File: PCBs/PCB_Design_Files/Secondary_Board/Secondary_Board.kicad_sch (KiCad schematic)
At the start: 0 parts

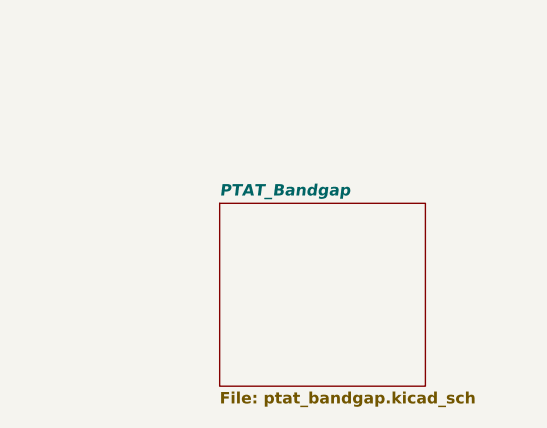
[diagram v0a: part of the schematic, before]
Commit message: ptat_bandgap schematic on secondary board
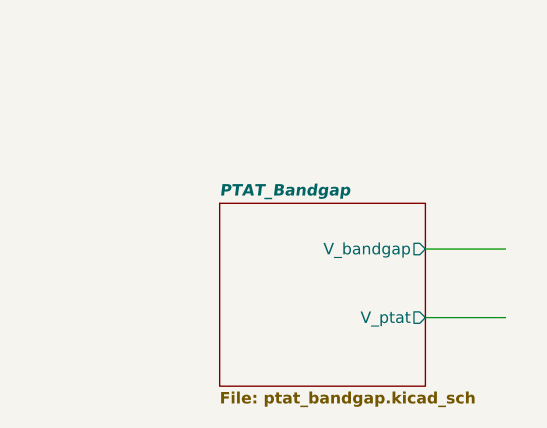
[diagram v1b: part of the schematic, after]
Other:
- sheet PTAT_Bandgap ports: added V_bandgap, V_ptat; removed none
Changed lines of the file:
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@@
+		)
+	)
+	(wire
+		(pts
+			(xy 228.6 85.09) (xy 237.49 85.09)
+		)
+		(stroke
+			(width 0)
+			(type default)
+		)
+	)
+	(wire
+		(pts
+			(xy 228.6 92.71) (xy 237.49 92.71)
+		)
+		(stroke
+			(width 0)
+			(type default)
 		)
 	)
@@
 			)
 		)
+		(pin "V_bandgap" output
+			(at 228.6 85.09 0)
+			(effects
+				(font
+					(size 1.27 1.27)
+				)
+				(justify right)
+			)
+		)
+		(pin "V_ptat" output
+			(at 228.6 92.71 0)
+			(effects
+				(font
+					(size 1.27 1.27)
+				)
+				(justify right)
+			)
+		)

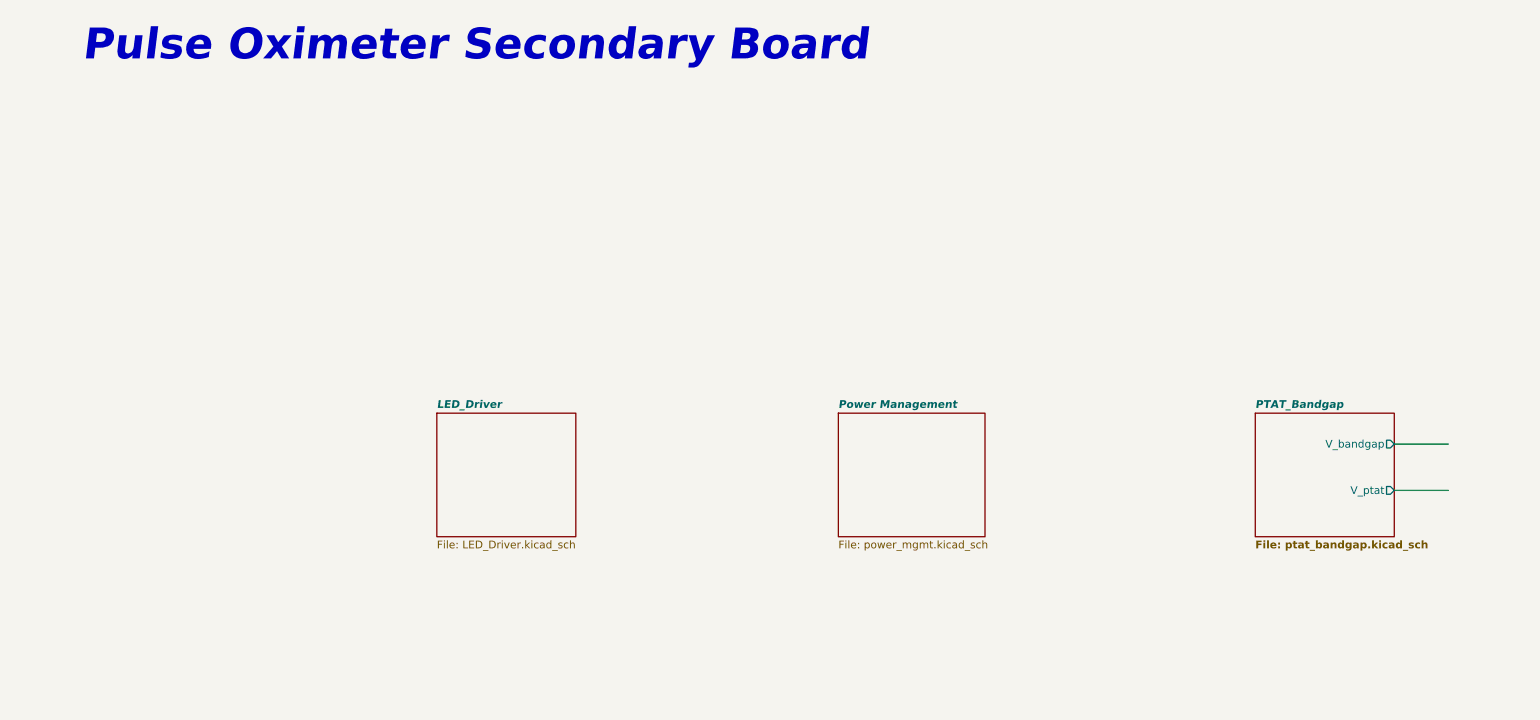
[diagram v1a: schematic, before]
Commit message: Bandgap/Ptat layout on secondary board. Updated grounded mounting holes on schematic, fix all DRC warnings
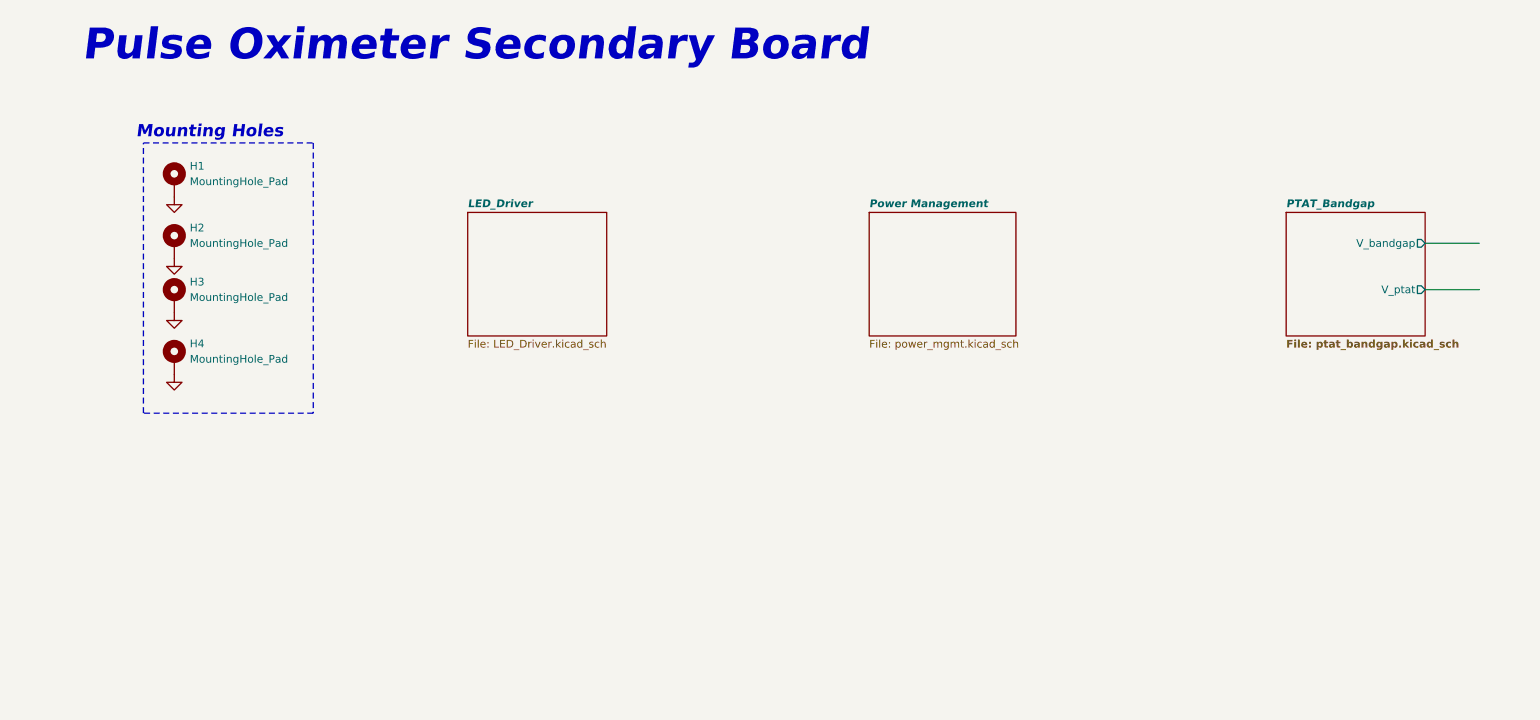
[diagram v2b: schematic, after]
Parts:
- added H1, H2, H3, H4: MountingHole_Pad, MountingHole:MountingHole_2.2mm_M2_DIN965_Pad, symbol Mechanical:MountingHole_Pad
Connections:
- new net GND: H1.1, H2.1, H3.1, H4.1
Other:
- note added: "Mounting Holes"

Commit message: Added header and ffc connector to both boards + update libraries. Updated BOM
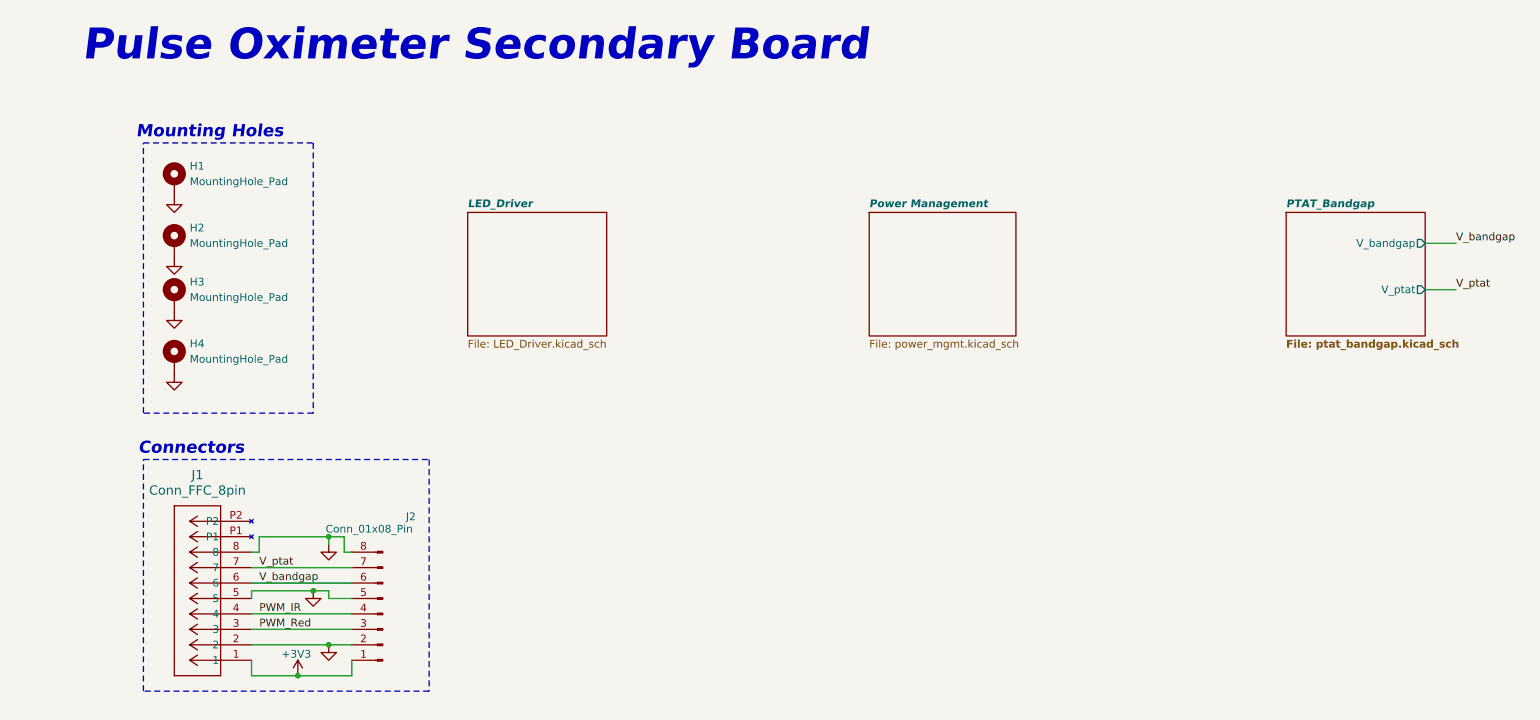
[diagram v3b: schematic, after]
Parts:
- added J1: Conn_FFC_8pin, Project Footprints:Conn_FFC_8pin, symbol Project_Symbols:Conn_FFC_8pin
- added J2: Conn_01x08_Pin, Connector_PinHeader_2.54mm:PinHeader_1x08_P2.54mm_Vertical, symbol Connector:Conn_01x08_Pin
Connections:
- net GND: now also J1.2, J1.5, J1.8, J2.2 (Pin_2), J2.5 (Pin_5), J2.8 (Pin_8)
- new net +3V3: J1.1, J2.1 (Pin_1)
- new net PWM_IR: J1.4, J2.4 (Pin_4)
- new net PWM_Red: J1.3, J2.3 (Pin_3)
- new net V_bandgap: J1.6, J2.6 (Pin_6)
- new net V_ptat: J1.7, J2.7 (Pin_7)
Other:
- note added: "Connectors"

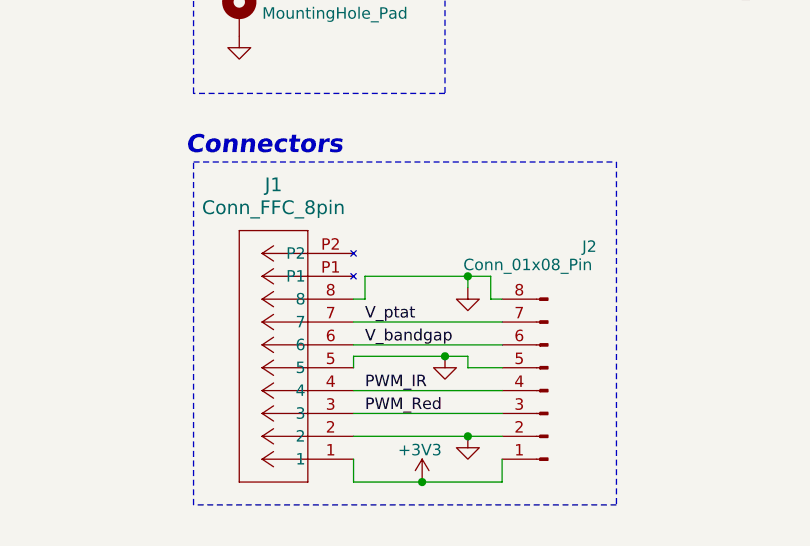
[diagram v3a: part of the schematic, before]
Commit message: pin 2 5V
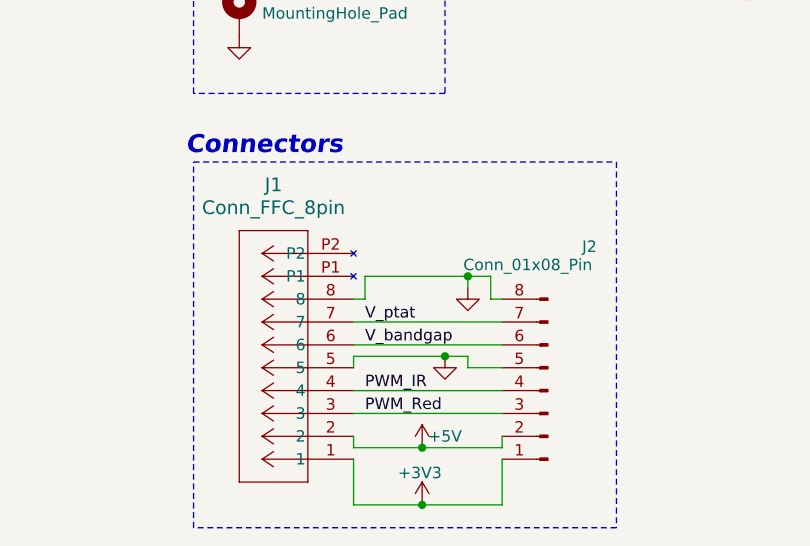
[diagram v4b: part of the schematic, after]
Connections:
- net GND: no longer J1.2, J2.2 (Pin_2)
- new net +5V: J1.2, J2.2 (Pin_2)
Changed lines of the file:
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@@
 	(rectangle
 		(start 22.86 87.63)
-		(end 69.85 125.73)
+		(end 69.85 128.27)
 		(stroke
 			(width 0)
@@
 	)
 	(junction
-		(at 48.26 123.19)
+		(at 50.8 109.22)
 		(diameter 0)
 		(color 0 0 0 0)
 	)
 	(junction
-		(at 50.8 109.22)
+		(at 48.26 119.38)
 		(diameter 0)
 		(color 0 0 0 0)
@@
 	)
 	(junction
-		(at 53.34 118.11)
+		(at 48.26 125.73)
 		(diameter 0)
 		(color 0 0 0 0)
@@
 	(wire
 		(pts
+			(xy 48.26 119.38) (xy 57.15 119.38)
+		)
+		(stroke
+			(width 0)
+			(type default)
+		)
+	)
+	(wire
+		(pts
 			(xy 50.8 109.22) (xy 53.34 109.22)
 		)
@@
 	(wire
 		(pts
-			(xy 40.64 120.65) (xy 40.64 123.19)
+			(xy 40.64 120.65) (xy 40.64 125.73)
 		)
 		(stroke
@@
 	(wire
 		(pts
-			(xy 40.64 123.19) (xy 48.26 123.19)
+			(xy 40.64 125.73) (xy 48.26 125.73)
 		)
 		(stroke
@@
 	(wire
 		(pts
-			(xy 57.15 123.19) (xy 48.26 123.19)
-		)
-		(stroke
-			(width 0)
-			(type default)
-		)
-	)
-	(wire
-		(pts
-			(xy 57.15 120.65) (xy 57.15 123.19)
+			(xy 57.15 125.73) (xy 48.26 125.73)
+		)
+		(stroke
+			(width 0)
+			(type default)
+		)
+	)
+	(wire
+		(pts
+			(xy 57.15 120.65) (xy 57.15 125.73)
 		)
 		(stroke
@@
 	(wire
 		(pts
-			(xy 53.34 118.11) (xy 57.15 118.11)
+			(xy 40.64 119.38) (xy 40.64 118.11)
 		)
 		(stroke
@@
 	(wire
 		(pts
-			(xy 40.64 118.11) (xy 53.34 118.11)
+			(xy 40.64 119.38) (xy 48.26 119.38)
+		)
+		(stroke
+			(width 0)
+			(type default)
+		)
+	)
+	(wire
+		(pts
+			(xy 57.15 119.38) (xy 57.15 118.11)
 		)
 		(stroke
@@
 	(symbol
 		(lib_id "power:+3V3")
-		(at 48.26 123.19 0)
+		(at 48.26 125.73 0)
 		(unit 1)
 		(exclude_from_sim no)
@@
 		(dnp no)
 		(property "Reference" "#PWR014"
-			(at 48.26 127 0)
+			(at 48.26 129.54 0)
 			(effects
 				(font
@@
 		)
 		(property "Value" "+3V3"
-			(at 48.006 119.634 0)
+			(at 48.006 122.174 0)
 			(effects
 				(font
@@
 		)
 		(property "Footprint" ""
-			(at 48.26 123.19 0)
+			(at 48.26 125.73 0)
 			(effects
 				(font
@@
 		)
 		(property "Datasheet" ""
-			(at 48.26 123.19 0)
+			(at 48.26 125.73 0)
 			(effects
 				(font
@@
 		)
 		(property "Description" "Power symbol creates a global label with name \"+3V3\""
-			(at 48.26 123.19 0)
+			(at 48.26 125.73 0)
 			(effects
 				(font
@@
 				(path "/2f5986e4-77b2-4f5d-ab91-80ba6228eb8b"
 					(reference "#PWR014")
-					(unit 1)
-				)
-			)
-		)
-	)
-	(symbol
-		(lib_id "power:GND")
-		(at 53.34 118.11 0)
-		(unit 1)
-		(exclude_from_sim no)
-		(in_bom yes)
-		(on_board yes)
-		(dnp no)
-		(fields_autoplaced yes)
-		(property "Reference" "#PWR017"
-			(at 53.34 124.46 0)
-			(effects
-				(font
-					(size 1.27 1.27)
-				)
-				(hide yes)
-			)
-		)
-		(property "Value" "GND"
-			(at 53.3401 121.92 90)
-			(effects
-				(font
-					(size 1.27 1.27)
-				)
-				(justify right)
-				(hide yes)
-			)
-		)
-		(property "Footprint" ""
-			(at 53.34 118.11 0)
-			(effects
-				(font
-					(size 1.27 1.27)
-				)
-				(hide yes)
-			)
-		)
-		(property "Datasheet" ""
-			(at 53.34 118.11 0)
-			(effects
-				(font
-					(size 1.27 1.27)
-				)
-				(hide yes)
-			)
-		)
-		(property "Description" "Power symbol creates a global label with name \"GND\" , ground"
-			(at 53.34 118.11 0)
-			(effects
-				(font
-					(size 1.27 1.27)
-				)
-				(hide yes)
-			)
-		)
-		(pin "1"
-		)
-		(instances
-			(project "Secondary_Board"
-				(path "/2f5986e4-77b2-4f5d-ab91-80ba6228eb8b"
-					(reference "#PWR017")
 					(unit 1)
 				)
@@
 					(unit 1)
 				)
+			)
+		)
+	)
+	(symbol
+		(lib_id "power:VCC")
+		(at 48.26 119.38 0)
+		(unit 1)
+		(exclude_from_sim no)
+		(in_bom yes)
+		(on_board yes)
+		(dnp no)
+		(property "Reference" "#PWR017"
+			(at 48.26 123.19 0)
+			(effects
+				(font
+					(size 1.27 1.27)
+				)
+				(hide yes)
+			)
+		)
+		(property "Value" "+5V"
+			(at 50.8 118.11 0)
+			(effects
+				(font
+					(size 1.27 1.27)
+				)
+			)
+		)
+		(property "Footprint" ""
+			(at 48.26 119.38 0)
+			(effects
+				(font
+					(size 1.27 1.27)
+				)
+				(hide yes)
+			)
+		)
+		(property "Datasheet" ""
+			(at 48.26 119.38 0)
+			(effects
+				(font
+					(size 1.27 1.27)
+				)
+				(hide yes)
+			)
+		)
+		(property "Description" "Power symbol creates a global label with name \"VCC\""
+			(at 48.26 119.38 0)
+			(effects
+				(font
+					(size 1.27 1.27)
+				)
+				(hide yes)
+			)
+		)
+		(pin "1"
+		)
+		(instances
+			(project "Secondary_Board"
+				(path "/2f5986e4-77b2-4f5d-ab91-80ba6228eb8b"
+					(reference "#PWR017")
+					(unit 1)
+				)

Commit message: updated bg_ptat
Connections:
- net V_bandgap: now also J1.7, J2.7 (Pin_7); no longer J1.6, J2.6 (Pin_6)
- net V_ptat: now also J1.6, J2.6 (Pin_6); no longer J1.7, J2.7 (Pin_7)
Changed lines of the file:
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@@
 		)
 	)
-	(label "V_bandgap"
+	(label "V_ptat"
 		(at 41.91 107.95 0)
 		(effects
@@
 	)
 	(label "V_bandgap"
+		(at 41.91 105.41 0)
+		(effects
+			(font
+				(size 1.27 1.27)
+			)
+			(justify left bottom)
+		)
+	)
+	(label "V_bandgap"
 		(at 238.76 52.07 0)
 		(effects
@@
 		(effects
 			(font
-				(size 1.27 1.27)
-			)
-			(justify left bottom)
-		)
-	)
-	(label "V_ptat"
-		(at 41.91 105.41 0)
-		(effects
-			(font

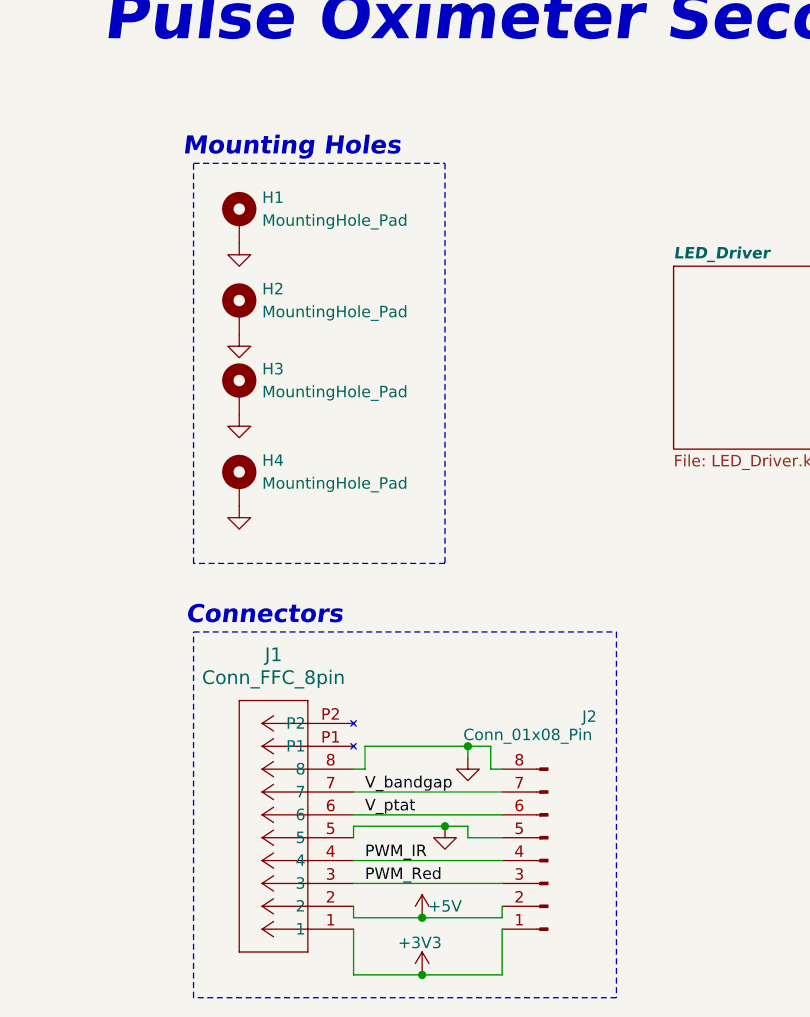
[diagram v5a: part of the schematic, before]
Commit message: connected connectors
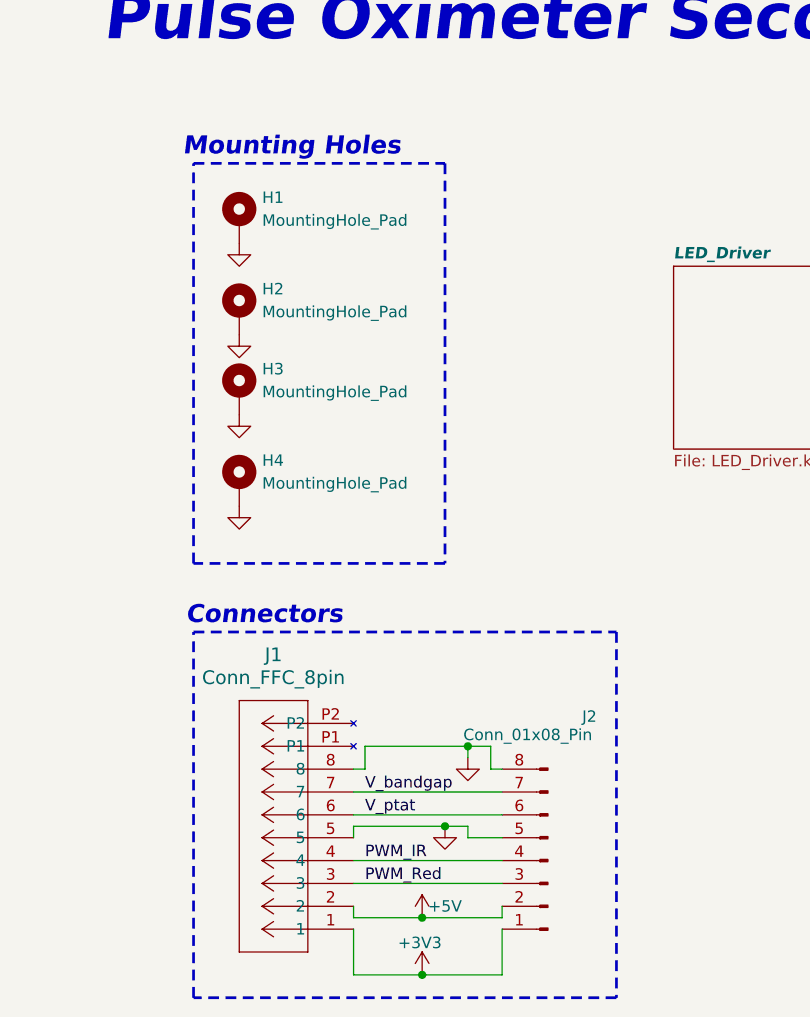
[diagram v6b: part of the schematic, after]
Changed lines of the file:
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@@
 		(end 50.8 80.01)
 		(stroke
-			(width 0)
+			(width 0.3)
 			(type dash)
+			(color 0 0 0 1)
 		)
 		(fill
@@
 		(end 69.85 128.27)
 		(stroke
-			(width 0)
+			(width 0.3)
 			(type dash)
+			(color 0 0 0 1)
 		)
 		(fill

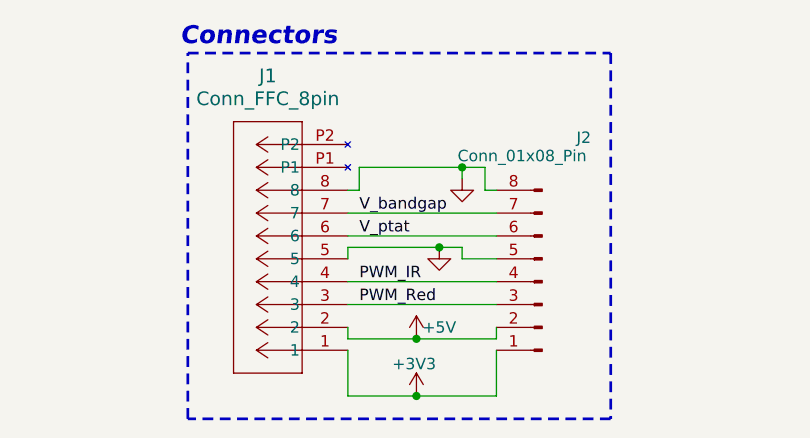
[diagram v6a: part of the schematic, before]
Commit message: LED Driver added to PCB
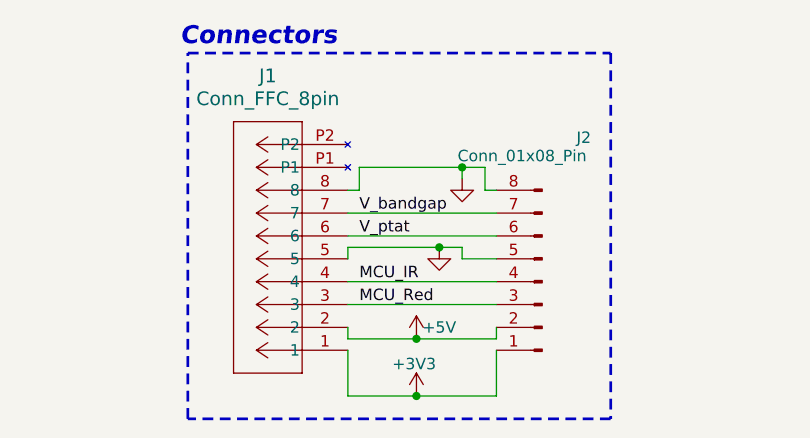
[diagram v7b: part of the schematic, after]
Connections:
- net PWM_IR renamed MCU_IR
- net PWM_Red renamed MCU_Red
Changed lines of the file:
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@@
 		)
 	)
-	(label "PWM_IR"
+	(label "MCU_IR"
 		(at 41.91 113.03 0)
 		(effects
@@
 		)
 	)
-	(label "PWM_Red"
+	(label "MCU_Red"
 		(at 41.91 115.57 0)
 		(effects

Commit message: LED Driver Updates
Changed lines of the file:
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@@
-		)
-	)
-	(label "MCU_IR"
-		(at 41.91 113.03 0)
-		(effects
-			(font
-				(size 1.27 1.27)
-			)
-			(justify left bottom)
 		)
 	)
@@
 		)
 	)
-	(label "MCU_Red"
-		(at 41.91 115.57 0)
+	(global_label "MCU_IR"
+		(shape input)
+		(at 41.91 113.03 180)
+		(fields_autoplaced yes)
 		(effects
 			(font
 				(size 1.27 1.27)
 			)
-			(justify left bottom)
+			(justify right)
+		)
+		(property "Intersheetrefs" "${INTERSHEET_REFS}"
+			(at 32.0305 113.03 0)
+			(effects
+				(font
+					(size 1.27 1.27)
+				)
+				(justify right)
+				(hide yes)
+			)
 		)
 	)
+	(global_label "MCU_Red"
+		(shape input)
+		(at 41.91 115.57 180)
+		(fields_autoplaced yes)
+		(effects
+			(font
+				(size 1.27 1.27)
+			)
+			(justify right)
+		)
+		(property "Intersheetrefs" "${INTERSHEET_REFS}"
+			(at 30.3977 115.57 0)
+			(effects
+				(font
+					(size 1.27 1.27)
+				)
+				(justify right)
+				(hide yes)
+			)
+		)
+	)
